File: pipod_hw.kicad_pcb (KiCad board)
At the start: 4 copper layers, 55.5 x 96.8 mm, 138 parts, among them J1 Conn_01x03_Male, J2 USB_C_Receptacle_USB2.0, J3 SFV8R-2STE1HLF, J4 SFV14R-2STE1HLF, J5 2-1734839-5, Q1 DMG9926UDM, Q2 NTK3139PT1G, Q3 BSS138, U1 MAX17048G+T10, U10 TPS22965TDSGRQ1, U11 TPS22965TDSGRQ1, U12 TPS22965TDSGRQ1, U13 PCM5102APWR, U14 PAM8908JER, U15 MCP23008-E/ML, U2 MAX8903AETI+T, U3 BQ29728DSER, U4 XC6210B332MR, U5 W25Q128JVS, U6 RP2040, U7 NLAS7242MUTBG, U8 RS2299XTQC16, U9 TPS22965TDSGRQ1, Y1 12MHz 20pF

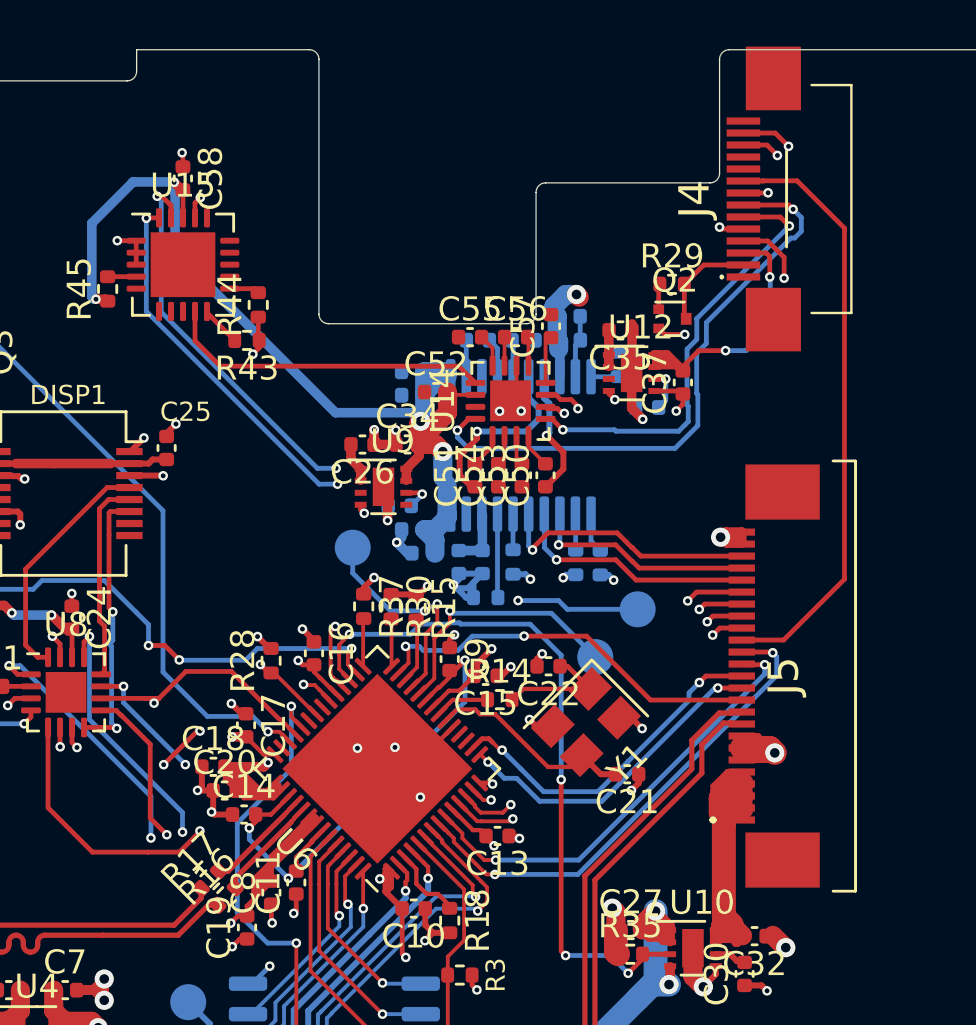
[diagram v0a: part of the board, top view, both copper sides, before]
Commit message: routing: finish routing (board is not manufacturable)
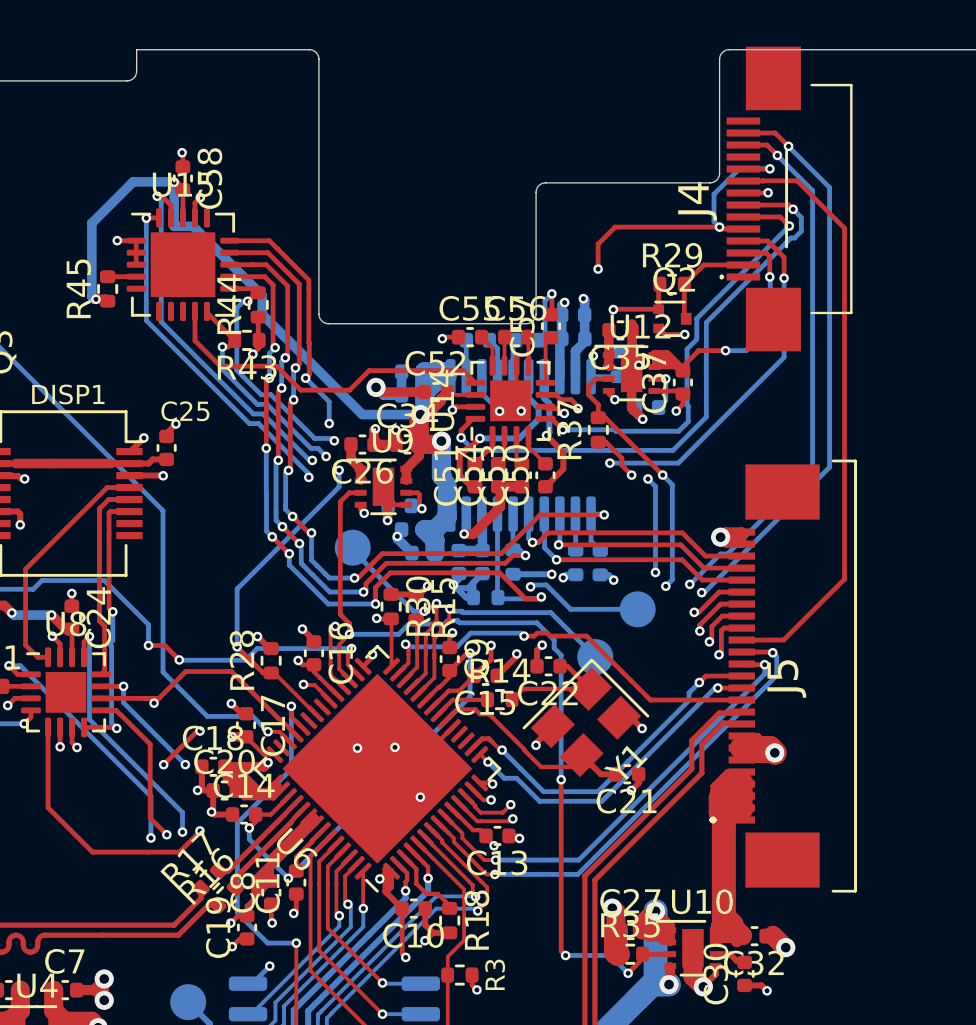
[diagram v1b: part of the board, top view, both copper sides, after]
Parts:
- moved R37 12.2 mm to (33.3, 15.8), turned to 90 degrees
- moved C40 0.20 mm to (32.3, 12.1)
- moved C41 0.20 mm to (32.2, 11.1)
- moved C46 0.15 mm to (30.3, 12.1)
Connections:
- U15 pad 12: PI_DAC_FMT -> PI_DAC_XSMT
- U15 pad 13: PI_DAC_XSMT -> PI_DAC_FMT
- U15 pad 14: PI_DAC_DEMP -> PI_DAC_FLT
- U15 pad 15: PI_DAC_FLT -> PI_DAC_DEMP
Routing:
- net SMC_RMT_RX: track 3.47 -> 43.8 mm, vias 2 -> 3
- net SMC_RMT_TX: track 4.46 -> 43.4 mm, vias 2 -> 3
- net HP_LCK: track 6.00 -> 40.9 mm, vias 2 -> 4
- net PI_DAC_FLT: track 1.67 -> 31.5 mm, vias 0 -> 7
- net HP_CLICKER: track 3.04 -> 32.1 mm, vias 0 -> 4
- net PI_DAC_XSMT: track 3.49 -> 32.2 mm, vias 0 -> 7
- net PI_DAC_FMT: track 1.49 -> 27.7 mm, vias 0 -> 7
- net PI_DAC_DEMP: track 1.13 -> 25.3 mm, vias 0 -> 3
- net RMT_3V3_EN: track 2.00 -> 25.9 mm, vias 0 -> 3
- net GNDA: track 1.03 -> 23.8 mm, vias 1 -> 4
- net PI_AMP_G1: track 2.90 -> 23.5 mm, vias 1 -> 3
- net GND: track 170.8 -> 190.9 mm, vias 84 -> 90
- net PI_AMP_G0: track 2.58 -> 21.2 mm, vias 1 -> 3
- net PI_VCC_EN: track 29.5 -> 36.5 mm
- net AUDIO_3V3: track 60.6 -> 57.6 mm
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
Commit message: layout, routing: relayout and reroute board
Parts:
- removed H3, H4: 9774040243R, Gigahawk:9774040243R
- added R46: 10k, Resistor_SMD:R_0402_1005Metric, F.Cu at (10.5, 31.4)
- added R47: 10k, Resistor_SMD:R_0402_1005Metric, F.Cu at (12.4, 32.1)
- C12, C29, C36, R12, R13: moved to F.Cu
- U5: footprint Package_SO:SOIC-8_5.23x5.23mm_P1.27mm -> Package_SON:WSON-8-1EP_6x5mm_P1.27mm_EP3.4x4.3mm; moved to F.Cu
- Y1: footprint Crystal:Crystal_SMD_3225-4Pin_3.2x2.5mm -> Crystal:Crystal_SMD_2520-4Pin_2.5x2.0mm
- moved R45 46.2 mm to (46.2, 42.0), turned to 0 degrees
- moved C58 42.8 mm to (42.6, 38.9), turned to 0 degrees
- moved U15 42.5 mm to (46.2, 38.9), turned to 90 degrees
- moved R44 39.1 mm to (49.5, 35.2), turned to -90 degrees
- moved R43 37.4 mm to (48.1, 35.2), turned to -90 degrees
- moved C29 25.7 mm to (50.7, 18.5), turned to 180 degrees
- moved C43 25.5 mm to (50.8, 27.0), turned to -90 degrees
- moved C42 25.4 mm to (49.9, 27.4), turned to -90 degrees
- moved R28 24.2 mm to (36.4, 7.98), turned to 180 degrees
- moved R41 24.1 mm to (52.7, 24.4), turned to 90 degrees
- moved C49 24.1 mm to (51.2, 25.5), turned to 0 degrees
- moved C26 23.7 mm to (47.2, 16.2)
- moved C34 23.7 mm to (49.1, 16.2)
- moved U9 23.7 mm to (48.1, 18.0)
- moved C48 23.0 mm to (51.2, 24.5), turned to 0 degrees
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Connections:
- net Net-(C21-Pad2) renamed /SMC/SMC_XIN
- net Net-(C22-Pad1) renamed /SMC/SMC_XOUT_ATTN
- net Net-(C29-Pad2) renamed /Load Switches/AUDIO_SW_CT
- net Net-(C3-Pad1) renamed /Power/CHRG_LX
- net Net-(C3-Pad2) renamed /Power/CHRG_BST
- net Net-(C30-Pad2) renamed /Load Switches/PI_SW_CT
- net Net-(C31-Pad2) renamed /Load Switches/DISP_SW_CT
- net Net-(C36-Pad2) renamed /Load Switches/RMT_SW_CT
- net Net-(C4-Pad2) renamed /Power/CHRG_VL
- net Net-(C45-Pad1) renamed /Audio/DAC_CAPP
- net Net-(C45-Pad2) renamed /Audio/DAC_CAPM
- net Net-(C46-Pad1) renamed /Audio/DAC_VNEG
- net Net-(C48-Pad1) renamed /Audio/DAC_LDOO
- net Net-(C50-Pad2) renamed /Audio/AMP_INR-
- net Net-(C51-Pad2) renamed /Audio/AMP_INL-
- net Net-(C53-Pad2) renamed /Audio/AMP_INR+
- net Net-(C54-Pad2) renamed /Audio/AMP_INL+
- net Net-(C55-Pad2) renamed /Audio/AMP_HPVDD
- net Net-(C56-Pad1) renamed /Audio/AMP_CAP+
- net Net-(C56-Pad2) renamed /Audio/AMP_CAP-
- net Net-(C57-Pad1) renamed /Audio/AMP_HPVSS
- net Net-(D1-Pad1) renamed /Power/CHRG_FLT_LEDK
- net Net-(D2-Pad1) renamed /Power/CHRG_LEDK
- net Net-(D3-Pad1) renamed /Power/CHRG_DOK_LEDK
- net Net-(DISP1-Pad2) renamed /Display/DISP_LEDK
- net Net-(DISP1-Pad8) renamed /Display/DISP_CS
- net Net-(J2-PadS1) renamed /USB/USB_SHIELD
- net Net-(L1-Pad1) renamed /Power/CHRG_CS
- net Net-(Q3-Pad3) renamed /Display/DISP_BL_MOS_D
- net Net-(R11-Pad2) renamed /Power/PROT_V-
- net Net-(R14-Pad1) renamed /SMC/SMC_XOUT
- net Net-(R38-Pad2) renamed /Audio/DAC_SCK
- net Net-(R45-Pad2) renamed /Pi/~{IO_EX_RST}
- J5 pad 12: SMC_TX_PI_RX -> SMC_RX_PI_TX
- J5 pad 13: SMC_RX_PI_TX -> SMC_TX_PI_RX
- J5 pad 14: SMC_PI_I2C_SCL -> SMC_PI_I2C_SDA
- J5 pad 15: SMC_PI_I2C_SDA -> SMC_PI_I2C_SCL
- J5 pad 21: PI_I2S_DIN -> PI_I2S_LRCK
- J5 pad 22: PI_I2S_BCK -> PI_I2S_DIN
- J5 pad 23: PI_I2S_LRCK -> PI_I2S_BCK
- Q1 pad 2: Net-(Q1-Pad2) -> unconnected-(Q1-Pad2)
- Q1 pad 5: Net-(Q1-Pad2) -> unconnected-(Q1-Pad5)
- U15 pad 10: PI_AMP_G0 -> PI_AMP_G1
- U15 pad 11: PI_AMP_G1 -> PI_AMP_G0
- U6 pad 11: SMC_DISP_DC -> SMC_PI_I2C_SDA
- U6 pad 12: SMC_DISP_RST -> SMC_PI_I2C_SCL
- U6 pad 13: SMC_DISP_SCK -> HP_CLICKER
- U6 pad 14: SMC_DISP_MOSI -> HP_LCK
- U6 pad 15: SMC_TX_PI_RX -> SMC_RMT_TX
- U6 pad 16: SMC_RX_PI_TX -> SMC_RMT_RX
- U6 pad 18: unconnected-(U6-Pad18) -> DISP_3V3_EN
- U6 pad 2: SMC_CW_MOSI -> PI_VCC_EN
- U6 pad 27: SMC_INT -> DISP_INPUT_SEL
- U6 pad 28: HP_CLICKER -> SMC_DISP_RST
- U6 pad 29: RMT_3V3_EN -> SMC_DISP_SCK
- U6 pad 3: /SMC/~{SMC_CW_CS} -> SMC_INT
- U6 pad 30: DISP_3V3_EN -> SMC_DISP_MOSI
- U6 pad 31: PI_VCC_EN -> SMC_DISP_DC
- U6 pad 32: SMC_RMT_TX -> SMC_DISP_BL
- U6 pad 34: SMC_RMT_RX -> SMC_I2C_SDA
- U6 pad 35: unconnected-(U6-Pad35) -> SMC_I2C_SCL
- U6 pad 36: HP_LCK -> RMT_3V3_EN
- U6 pad 37: unconnected-(U6-Pad37) -> /SMC/~{SMC_CW_CS}
- U6 pad 38: USB_DET -> SMC_CW_SCK
- U6 pad 39: DISP_INPUT_SEL -> ~{FG_ALRT}
- U6 pad 4: SMC_CW_SCK -> USB_MUX_SEL
- U6 pad 40: SMC_DISP_BL -> SMC_CW_MOSI
- U6 pad 41: unconnected-(U6-Pad41) -> USB_DET
- U6 pad 5: ~{FG_ALRT} -> unconnected-(U6-Pad5)
- U6 pad 6: SMC_I2C_SDA -> SMC_RX_PI_TX
- U6 pad 7: SMC_I2C_SCL -> SMC_TX_PI_RX
- U6 pad 8: SMC_PI_I2C_SDA -> unconnected-(U6-Pad8)
- U6 pad 9: SMC_PI_I2C_SCL -> unconnected-(U6-Pad9)
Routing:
- net GND: track 190.9 -> 127.9 mm, vias 90 -> 105
- net USB_MUX_SEL: track 1.29 -> 35.9 mm, vias 0 -> 4
- net +3V3: track 83.4 -> 55.7 mm, vias 25 -> 29
- net SMC_PI_I2C_SDA: track 59.2 -> 33.1 mm, vias 4 -> 2
- net USB_DET: track 102.8 -> 80.6 mm, vias 6 -> 2
- net SMC_PI_I2C_SCL: track 56.1 -> 34.2 mm, vias 4 -> 2
- net AUDIO_3V3: track 57.6 -> 79.0 mm, vias 5 -> 6
- net ~{FG_ALRT}: track 140.7 -> 119.6 mm, vias 6 -> 5
- net PI_AMP_EN: track 14.3 -> 34.7 mm, vias 0 -> 2
- net DISP_3V3_EN: track 27.4 -> 9.33 mm, vias 6 -> 2
- net SMC_DISP_RST: track 24.8 -> 7.85 mm, vias 2 -> 0
- net SMC_DISP_SCK: track 25.8 -> 10.2 mm, vias 3 -> 2
- net SMC_DISP_MOSI: track 24.8 -> 10.2 mm, vias 2 -> 0
- net VCC: track 142.9 -> 157.4 mm, vias 9 -> 10
- net PI_DAC_XSMT: track 32.2 -> 19.0 mm, vias 7 -> 1
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
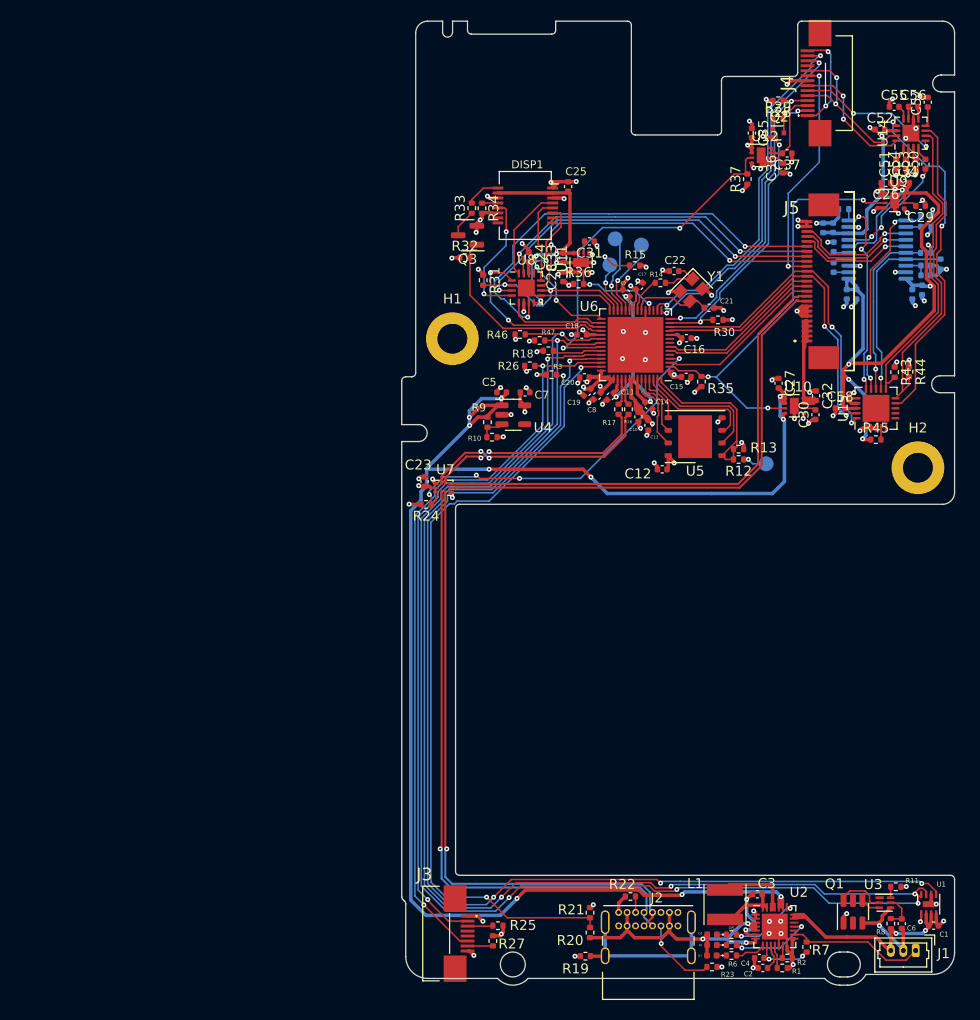
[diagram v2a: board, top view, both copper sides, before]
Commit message: layout: add testpoints, extra mounting hole, grounding clips
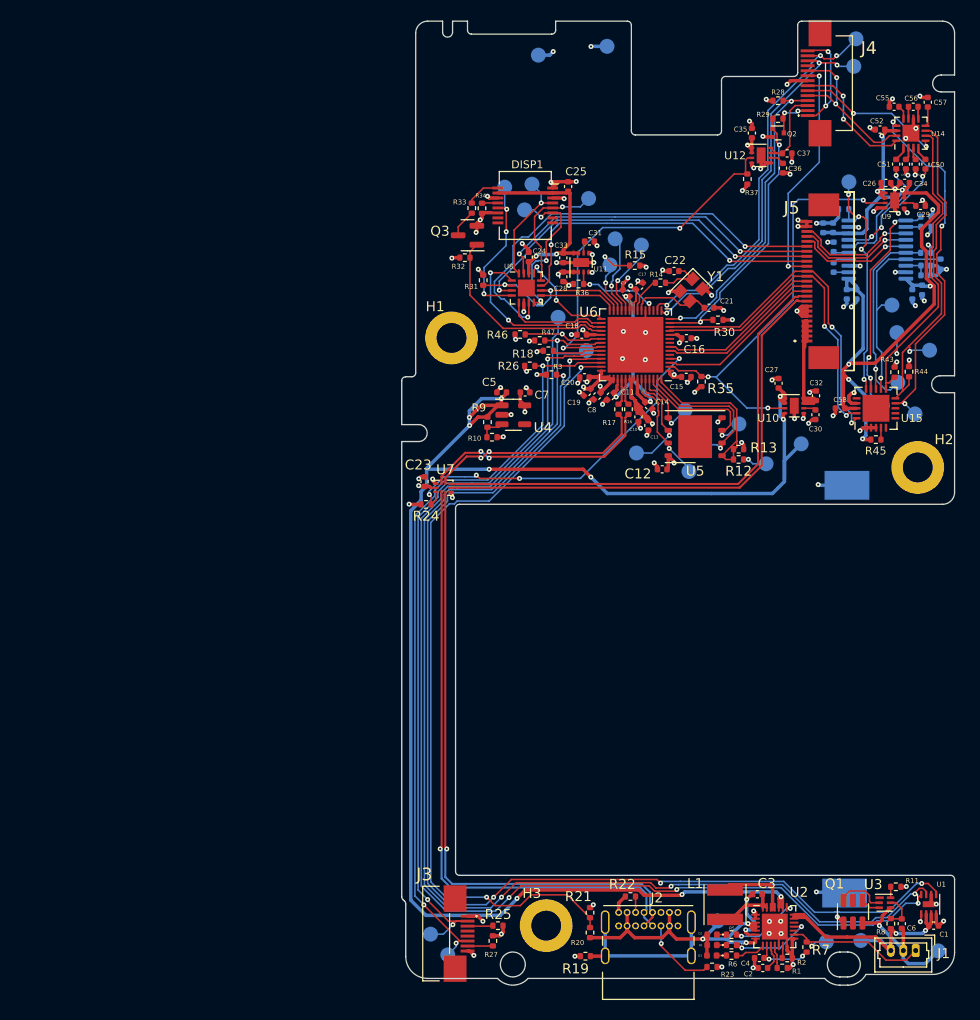
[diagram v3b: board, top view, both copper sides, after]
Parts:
- added H3: 9774040243R, Gigahawk:9774040243R, F.Cu at (13.1, 90.8)
- added J6: S7051-42R, Gigahawk:S705142R, B.Cu at (43.3, 46.6)
- added J7: S7051-42R, Gigahawk:S705142R, B.Cu at (43.1, 87.5)
- added TP10: TestPoint, TestPoint:TestPoint_Pad_D1.5mm, B.Cu at (12.3, 3.41)
- added TP11: TestPoint, TestPoint:TestPoint_Pad_D1.5mm, B.Cu at (19.2, 2.53)
- added TP12: TestPoint, TestPoint:TestPoint_Pad_D1.5mm, B.Cu at (22.2, 43.4)
- added TP13: TestPoint, TestPoint:TestPoint_Pad_D1.5mm, B.Cu at (50.1, 39.4)
- added TP14: TestPoint, TestPoint:TestPoint_Pad_D1.5mm, B.Cu at (51.6, 33.0)
- added TP15: TestPoint, TestPoint:TestPoint_Pad_D1.5mm, B.Cu at (48.3, 31.3)
- added TP16: TestPoint, TestPoint:TestPoint_Pad_D1.5mm, B.Cu at (44.0, 4.53)
- added TP17: TestPoint, TestPoint:TestPoint_Pad_D1.5mm, B.Cu at (44.2, 1.77)
- added TP18: TestPoint, TestPoint:TestPoint_Pad_D1.5mm, B.Cu at (11.7, 16.4)
- added TP19: TestPoint, TestPoint:TestPoint_Pad_D1.5mm, B.Cu at (8.94, 16.7)
- added TP20: TestPoint, TestPoint:TestPoint_Pad_D1.5mm, B.Cu at (10.9, 18.9)
- added TP21: TestPoint, TestPoint:TestPoint_Pad_D1.5mm, B.Cu at (17.4, 17.8)
- added TP22: TestPoint, TestPoint:TestPoint_Pad_D1.5mm, B.Cu at (14.3, 29.7)
- added TP23: TestPoint, TestPoint:TestPoint_Pad_D1.5mm, B.Cu at (17.1, 33.1)
- added TP24: TestPoint, TestPoint:TestPoint_Pad_D1.5mm, B.Cu at (27.0, 39.0)
- added TP25: TestPoint, TestPoint:TestPoint_Pad_D1.5mm, B.Cu at (29.0, 42.5)
- added TP26: TestPoint, TestPoint:TestPoint_Pad_D1.5mm, B.Cu at (32.4, 40.4)
- added TP27: TestPoint, TestPoint:TestPoint_Pad_D1.5mm, B.Cu at (27.4, 45.2)
- added TP28: TestPoint, TestPoint:TestPoint_Pad_D1.5mm, B.Cu at (47.8, 28.5)
- added TP29: TestPoint, TestPoint:TestPoint_Pad_D1.5mm, B.Cu at (48.4, 36.3)
- added TP30: TestPoint, TestPoint:TestPoint_Pad_D1.5mm, B.Cu at (46.9, 38.6)
- added TP31: TestPoint, TestPoint:TestPoint_Pad_D1.5mm, B.Cu at (43.5, 16.1)
- added TP32: TestPoint, TestPoint:TestPoint_Pad_D1.5mm, B.Cu at (1.49, 91.7)
- added TP33: TestPoint, TestPoint:TestPoint_Pad_D1.5mm, B.Cu at (3.22, 93.7)
- added TP5: TestPoint, TestPoint:TestPoint_Pad_D1.5mm, B.Cu at (41.2, 92.4)
- added TP6: TestPoint, TestPoint:TestPoint_Pad_D1.5mm, B.Cu at (52.4, 93.3)
- added TP7: TestPoint, TestPoint:TestPoint_Pad_D1.5mm, B.Cu at (44.7, 92.3)
- added TP8: TestPoint, TestPoint:TestPoint_Pad_D1.5mm, B.Cu at (38.7, 42.4)
- added TP9: TestPoint, TestPoint:TestPoint_Pad_D1.5mm, B.Cu at (30.3, 90.3)
- moved H1 0.11 mm to (3.60, 31.8)
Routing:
- net GND: track 127.9 -> 135.1 mm, vias 105 -> 108
- net SMC_I2C_SCL: track 122.4 -> 127.8 mm
- net -BATT: track 9.73 -> 14.8 mm
- net SMC_QSPI_SCLK: track 6.46 -> 11.1 mm, vias 0 -> 1
- net SMC_RMT_RX: track 35.9 -> 40.5 mm, vias 2 -> 3
- net DISP_SCK: track 8.64 -> 12.9 mm, vias 0 -> 1
- net SMC_CW_SCK: track 73.1 -> 77.3 mm, vias 2 -> 3
- net VCC: track 157.4 -> 161.7 mm
- net PI_DAC_DEMP: track 20.8 -> 24.9 mm, vias 3 -> 4
- net PI_DAC_FMT: track 17.5 -> 21.5 mm
- net SMC_QSPI_SD3: track 8.01 -> 11.7 mm, vias 0 -> 1
- net SMC_RMT_TX: track 34.6 -> 38.3 mm, vias 2 -> 3
- net SMC_I2C_SDA: track 126.1 -> 129.6 mm
- net +BATT: track 21.6 -> 25.1 mm
- net DISP_RST: track 12.5 -> 15.8 mm, vias 2 -> 3
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
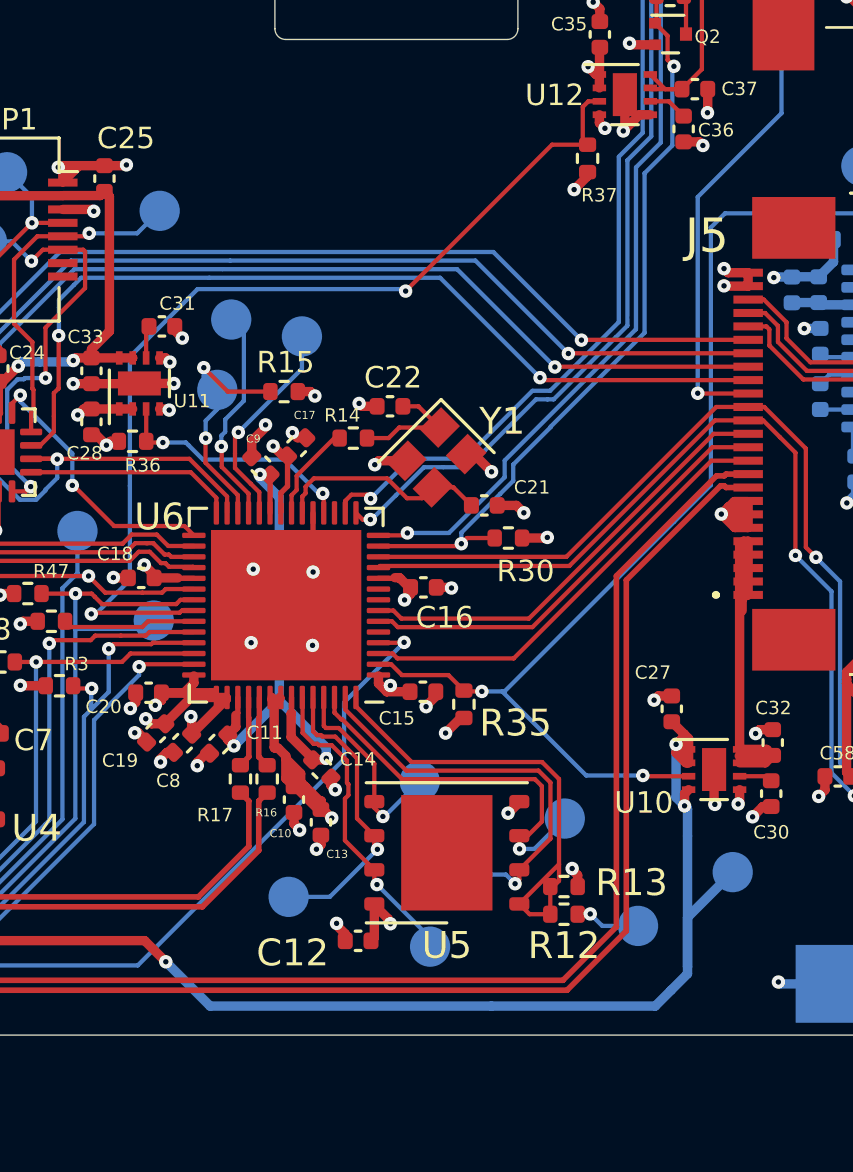
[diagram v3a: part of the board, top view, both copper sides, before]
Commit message: layout: cleanup silkscreen, add bootloader buttons
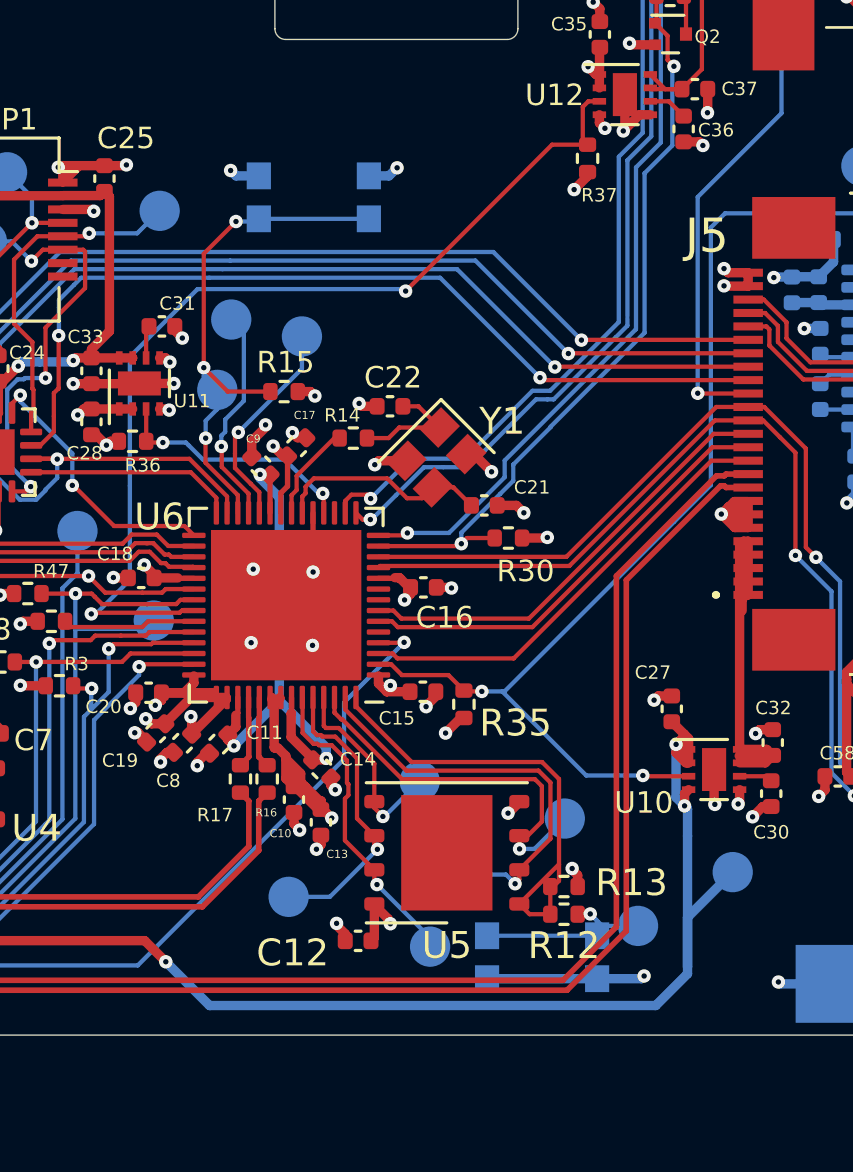
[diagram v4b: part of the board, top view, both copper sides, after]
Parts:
- added SW1: SW_Push, Gigahawk:SW_Push_1P1T_NO_CK_KMR2, B.Cu at (31.6, 45.6)
- added SW2: SW_Push, Gigahawk:SW_Push_1P1T_NO_CK_KMR2, B.Cu at (23.1, 17.3)
- R12: value 10k -> 1k
- R13: value DNP -> 10k
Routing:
- net MCU_RUN: track 9.15 -> 20.1 mm, vias 2 -> 3
- net GND: track 135.1 -> 143.3 mm, vias 108 -> 111
- net /SMC/~{SMC_USB_BOOT}: track 2.44 -> 7.46 mm
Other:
- board text added: "BOOTSEL"
- board text added: "RESET"
